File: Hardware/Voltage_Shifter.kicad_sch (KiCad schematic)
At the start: 25 parts, among them J2 Conn_02x08_Odd_Even, Q1 DMG3414U, Q2 DMG3414U, Q3 DMG3414U, Q4 DMG3414U, Q5 DMG3414U, Q6 DMG3414U, Q7 DMG3414U, Q8 DMG3414U

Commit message: [Hardware] Added the output voltage selection switch.
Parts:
- added SW1: ~, OS103011MA7QP1:OS103011MA7QP1, symbol OS103011MA7QP1:OS103011MA7QP1
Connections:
- net +5V: now also SW1.4
- net VCC: now also SW1.2
- new net +1V8: SW1.1
- new net +3.3V: SW1.2
- new net GND: SW1.5 (MH), SW1.6 (MH)
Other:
- note removed: "TODO : switch for VCC selection"

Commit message: [Hardware] Added a pin header connector to provide the output power supply.
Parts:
- J2: value Conn_02x08_Odd_Even -> I/O
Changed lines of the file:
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@@
 		(fields_autoplaced yes)
 		(property "Reference" "J2"
-			(at 49.53 172.72 0)
+			(at 49.53 144.78 0)
 			(effects
 				(font
@@
 			)
 		)
-		(property "Value" "Conn_02x08_Odd_Even"
-			(at 49.53 175.26 0)
+		(property "Value" "I/O"
+			(at 49.53 147.32 0)
 			(effects
 				(font
@@
 		)
 		(property "Description" "I/O"
-			(at 49.53 177.8 0)
+			(at 49.53 147.32 0)
 			(effects
 				(font
 					(size 1.27 1.27)
 				)
+				(hide yes)
 			)
 		)

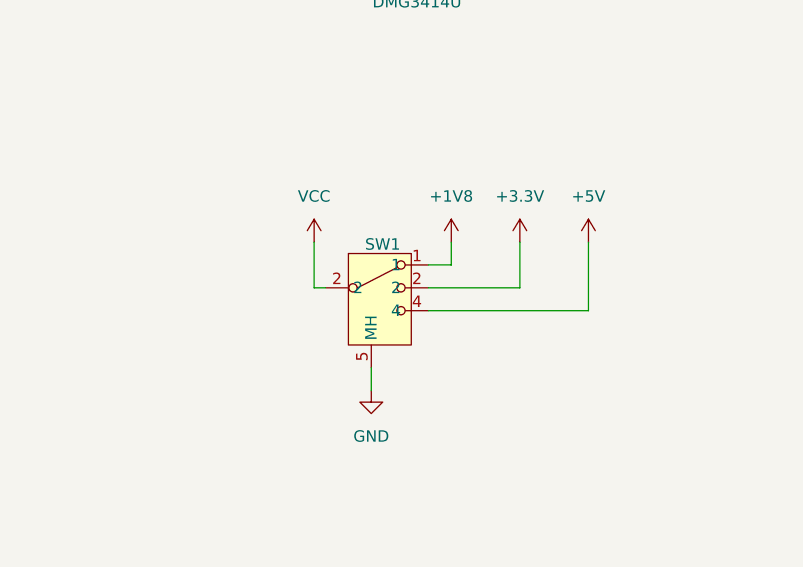
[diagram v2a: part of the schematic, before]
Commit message: [Hardware] Added the missing pin number 3 to the OS103011MA7QP1 switch.
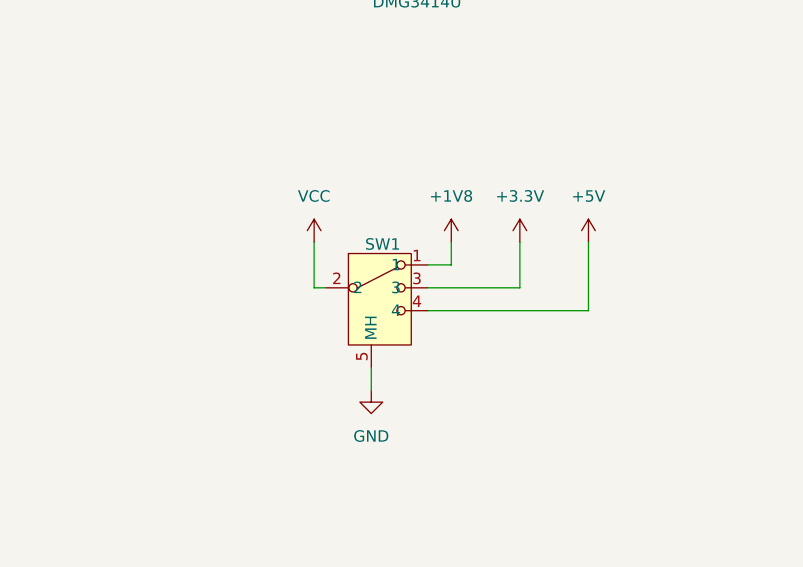
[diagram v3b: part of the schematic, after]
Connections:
- net +3.3V: now also SW1.3; no longer SW1.2
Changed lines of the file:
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@@
 		(pin "1"
 		)
-		(pin "2"
+		(pin "3"
 		)
 		(pin "2"

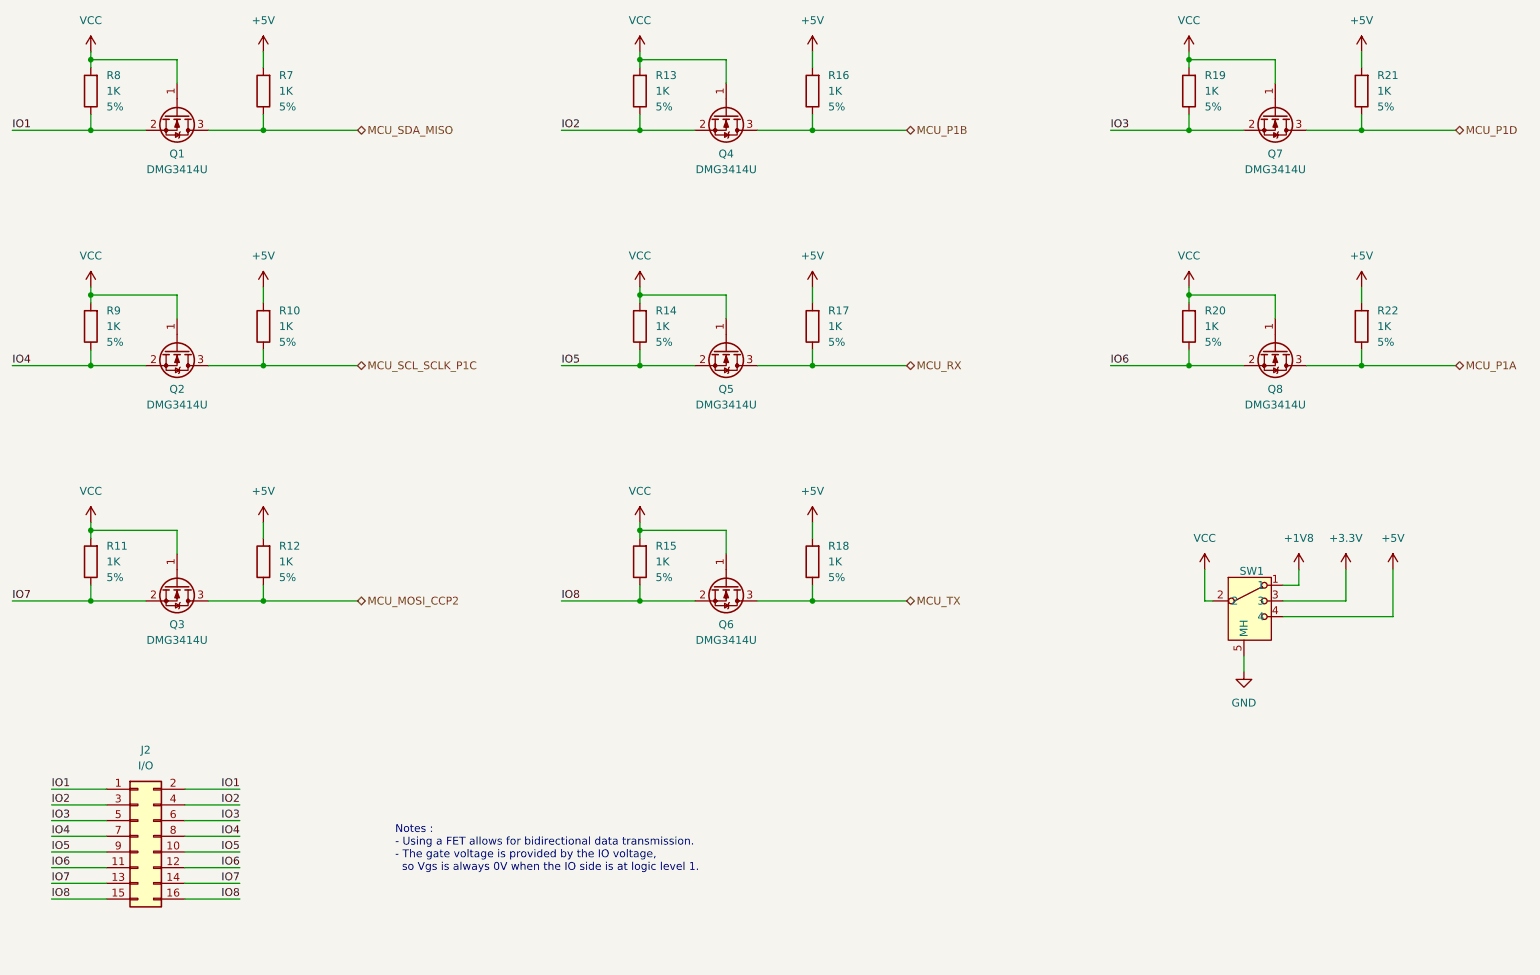
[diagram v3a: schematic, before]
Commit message: [Hardware] Routed all but the LEDs.
Changed the IOs order to help the routing.
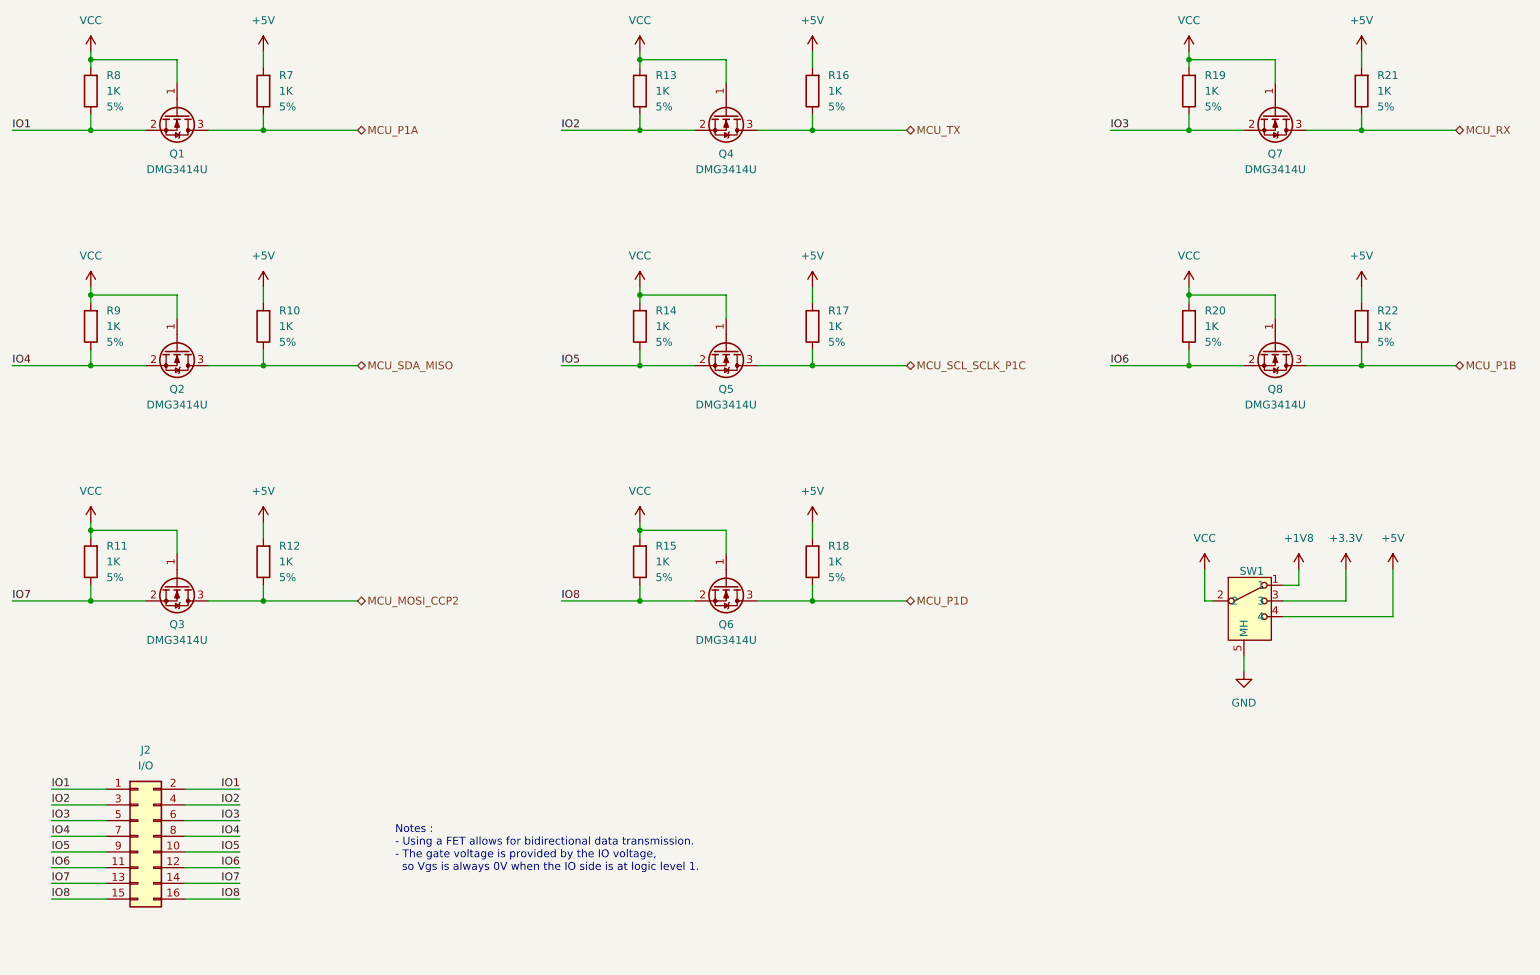
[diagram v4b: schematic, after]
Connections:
- net MCU_P1A: now also Q1.3 (D), R7.1; no longer Q8.3 (D), R22.1
- net MCU_P1B: now also Q8.3 (D), R22.1; no longer Q4.3 (D), R16.1
- net MCU_P1D: now also Q6.3 (D), R18.1; no longer Q7.3 (D), R21.1
- net MCU_RX: now also Q7.3 (D), R21.1; no longer Q5.3 (D), R17.1
- net MCU_SCL_SCLK_P1C: now also Q5.3 (D), R17.1; no longer Q2.3 (D), R10.1
- net MCU_SDA_MISO: now also Q2.3 (D), R10.1; no longer Q1.3 (D), R7.1
- net MCU_TX: now also Q4.3 (D), R16.1; no longer Q6.3 (D), R18.1
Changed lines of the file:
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@@
 	(hierarchical_label "MCU_P1A"
 		(shape bidirectional)
-		(at 261.62 82.55 0)
+		(at 83.82 44.45 0)
 		(effects
 			(font
@@
 	(hierarchical_label "MCU_SDA_MISO"
 		(shape bidirectional)
-		(at 83.82 44.45 0)
+		(at 83.82 82.55 0)
 		(effects
 			(font
@@
 	(hierarchical_label "MCU_SCL_SCLK_P1C"
 		(shape bidirectional)
-		(at 83.82 82.55 0)
+		(at 172.72 82.55 0)
 		(effects
 			(font
@@
 	(hierarchical_label "MCU_RX"
 		(shape bidirectional)
-		(at 172.72 82.55 0)
+		(at 261.62 44.45 0)
 		(effects
 			(font
@@
 	(hierarchical_label "MCU_P1D"
 		(shape bidirectional)
-		(at 261.62 44.45 0)
+		(at 172.72 120.65 0)
 		(effects
 			(font
@@
 	(hierarchical_label "MCU_P1B"
 		(shape bidirectional)
-		(at 172.72 44.45 0)
+		(at 261.62 82.55 0)
 		(effects
 			(font
@@
 	(hierarchical_label "MCU_TX"
 		(shape bidirectional)
-		(at 172.72 120.65 0)
+		(at 172.72 44.45 0)
 		(effects
 			(font

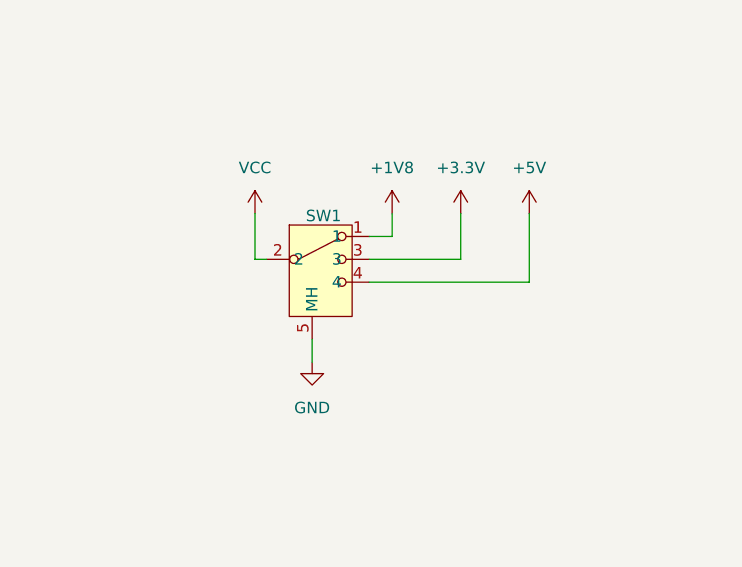
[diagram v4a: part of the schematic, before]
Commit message: [Hardware] Added the missing value for the switch into the schematic.
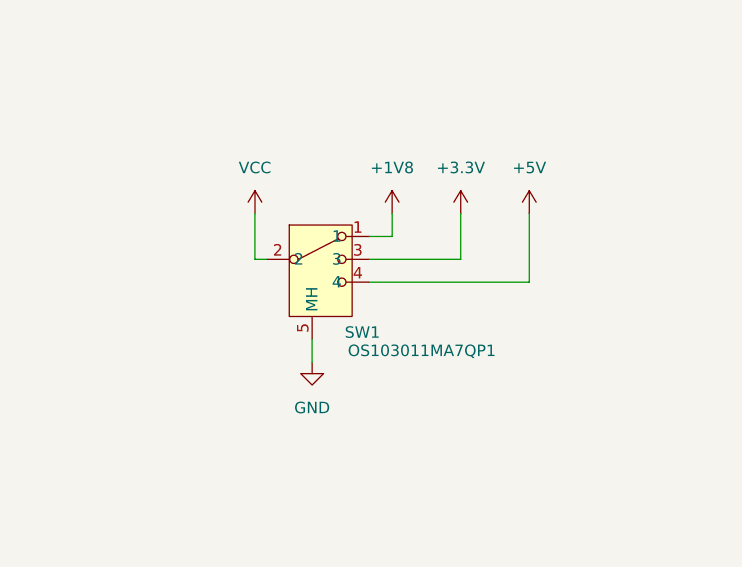
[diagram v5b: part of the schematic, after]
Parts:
- SW1: value ~ -> OS103011MA7QP1
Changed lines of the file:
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@@
 		(dnp no)
 		(property "Reference" "SW1"
-			(at 228.6 115.824 0)
+			(at 232.918 128.778 0)
 			(effects
 				(font
@@
 			)
 		)
-		(property "Value" "~"
-			(at 228.2825 115.57 0)
+		(property "Value" "OS103011MA7QP1"
+			(at 239.522 130.81 0)
 			(effects
 				(font
